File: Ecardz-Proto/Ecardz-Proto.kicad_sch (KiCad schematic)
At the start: 0 parts

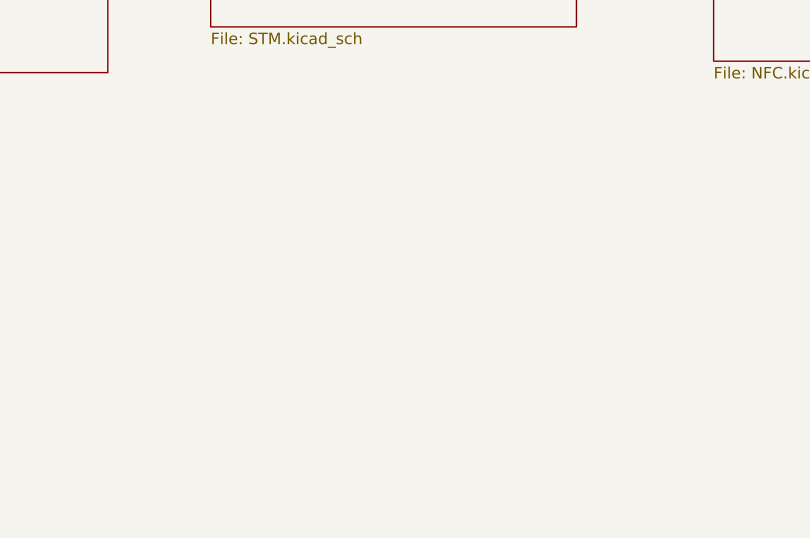
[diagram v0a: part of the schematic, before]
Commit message: added EEPROM schematic, removed personal files
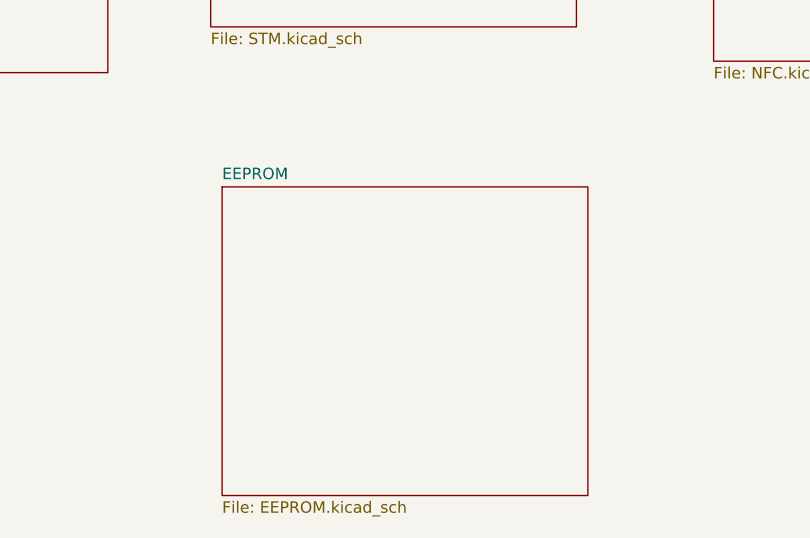
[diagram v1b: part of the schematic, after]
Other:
- added sheet EEPROM (EEPROM.kicad_sch)
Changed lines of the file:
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@@
+	)
+	(sheet
+		(at 114.3 115.57)
+		(size 40.64 34.29)
+		(fields_autoplaced yes)
+		(stroke
+			(width 0.1524)
+			(type solid)
+		)
+		(fill
+			(color 0 0 0 0.0000)
+		)
+		(property "Sheetname" "EEPROM"
+			(at 114.3 114.8584 0)
+			(effects
+				(font
+					(size 1.27 1.27)
+				)
+				(justify left bottom)
+			)
+		)
+		(property "Sheetfile" "EEPROM.kicad_sch"
+			(at 114.3 150.4446 0)
+			(effects
+				(font
+					(size 1.27 1.27)
+				)
+				(justify left top)
+			)
+		)
+		(instances
+			(project "Ecardz-Proto"
+				(path "/2adbba85-9270-4efb-857d-656bb51406ca"
+					(page "5")
+				)
+			)
+		)
 	)
 	(sheet

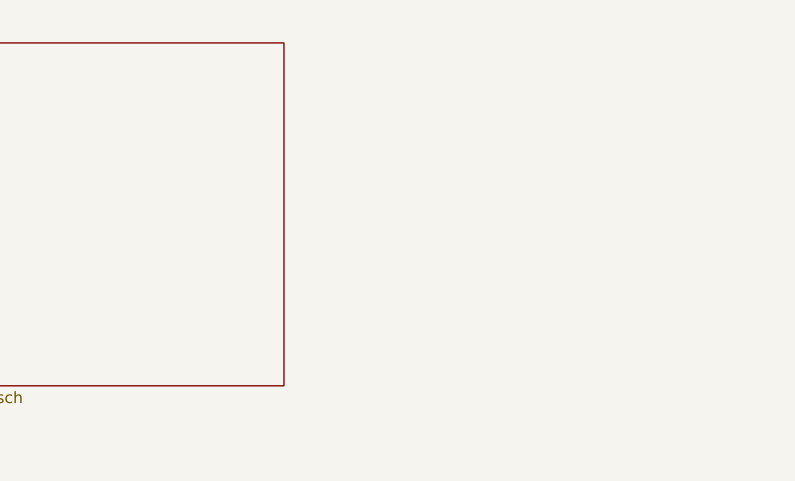
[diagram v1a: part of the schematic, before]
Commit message: added energy harvesting schematic page
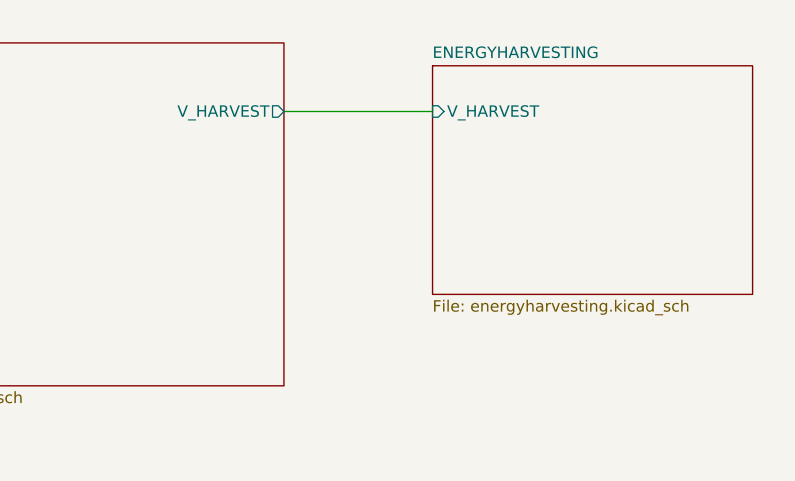
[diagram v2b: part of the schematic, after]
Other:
- added sheet ENERGYHARVESTING (energyharvesting.kicad_sch)
- sheet NFC ports: added V_HARVEST; removed none
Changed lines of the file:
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@@
+	(wire
+		(pts
+			(xy 214.63 71.12) (xy 231.14 71.12)
+		)
+		(stroke
+			(width 0)
+			(type default)
+		)
+	)
 	(wire
 		(pts
@@
 	)
 	(sheet
+		(at 231.14 66.04)
+		(size 35.56 25.4)
+		(fields_autoplaced yes)
+		(stroke
+			(width 0.1524)
+			(type solid)
+		)
+		(fill
+			(color 0 0 0 0.0000)
+		)
+		(property "Sheetname" "ENERGYHARVESTING"
+			(at 231.14 65.3284 0)
+			(effects
+				(font
+					(size 1.27 1.27)
+				)
+				(justify left bottom)
+			)
+		)
+		(property "Sheetfile" "energyharvesting.kicad_sch"
+			(at 231.14 92.0246 0)
+			(effects
+				(font
+					(size 1.27 1.27)
+				)
+				(justify left top)
+			)
+		)
+		(pin "V_HARVEST" input
+			(at 231.14 71.12 180)
+			(effects
+				(font
+					(size 1.27 1.27)
+				)
+				(justify left)
+			)
+		)
+		(instances
+			(project "Ecardz-Proto"
+				(path "/2adbba85-9270-4efb-857d-656bb51406ca"
+					(page "6")
+				)
+			)
+		)
+	)
+	(sheet
 		(at 168.91 63.5)
 		(size 45.72 38.1)
@@
 			)
 		)
+		(pin "V_HARVEST" output
+			(at 214.63 71.12 0)
+			(effects
+				(font
+					(size 1.27 1.27)
+				)
+				(justify right)
+			)
+		)

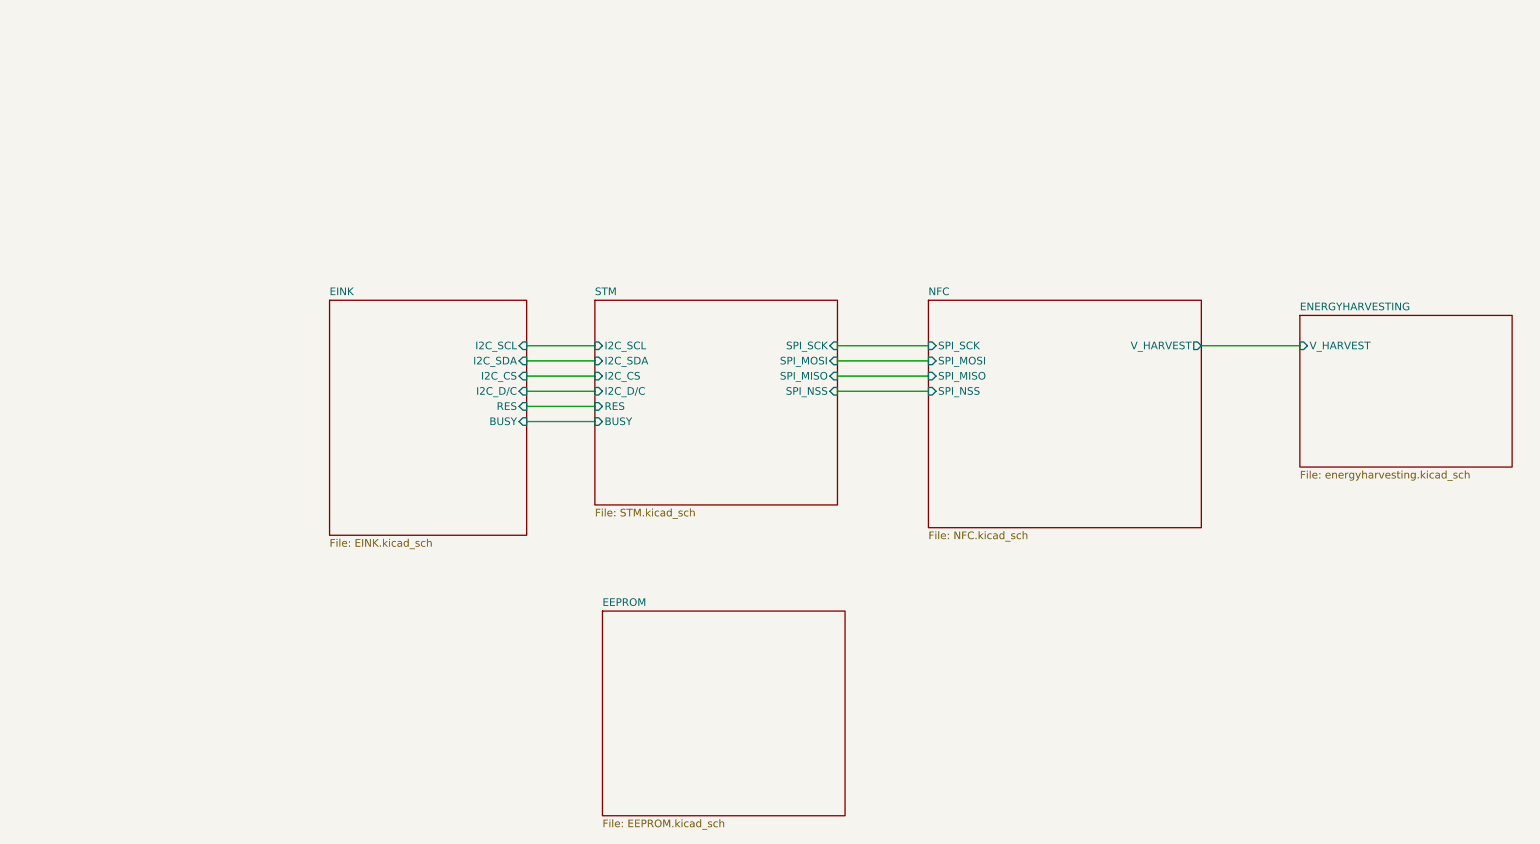
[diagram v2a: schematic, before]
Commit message: added energy harvesting sensing ADC to NFC
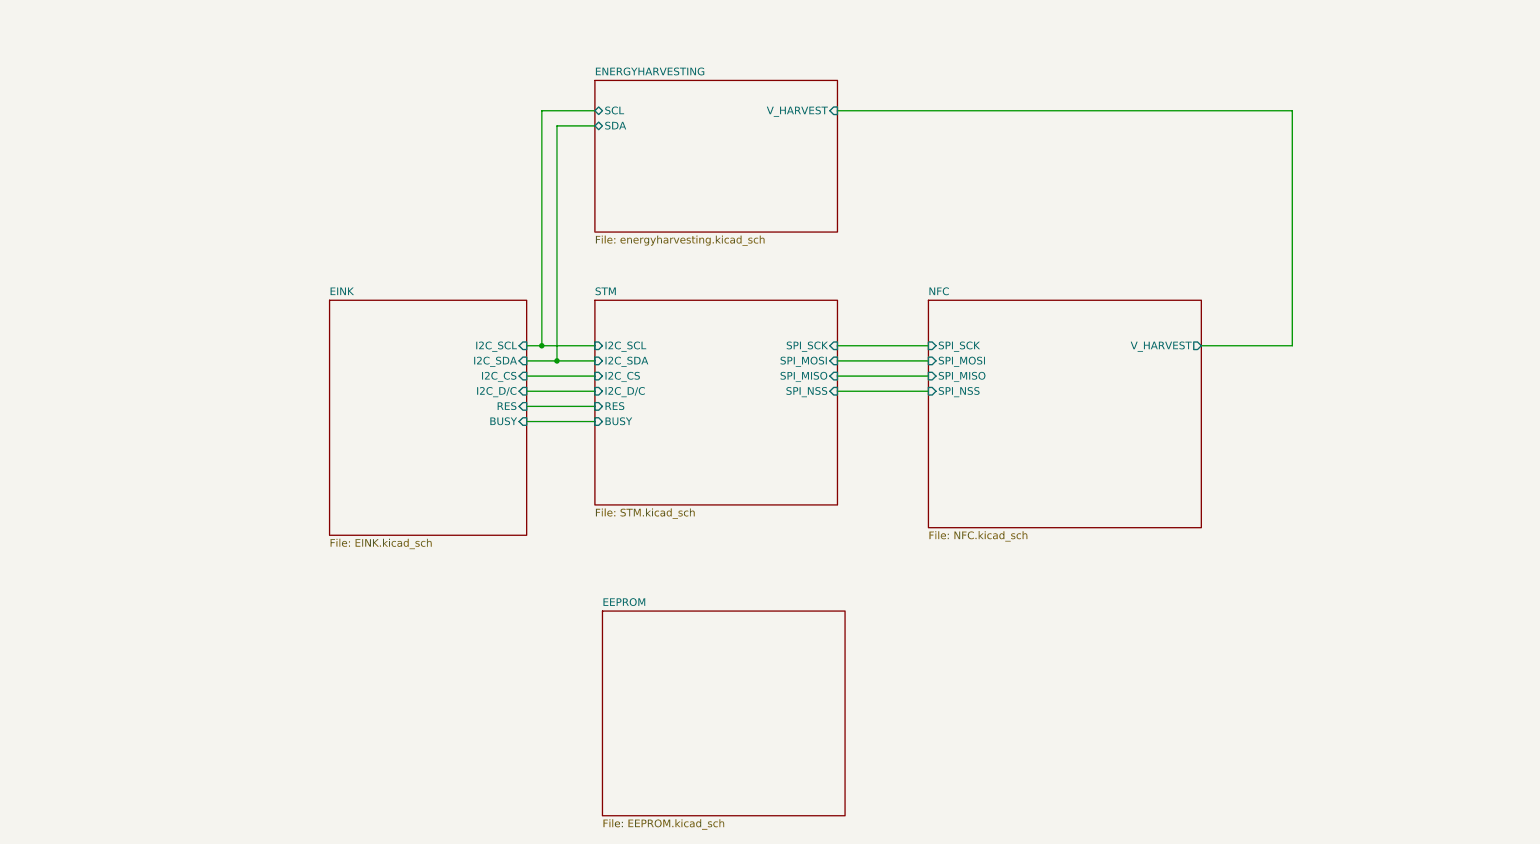
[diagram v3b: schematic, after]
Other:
- sheet ENERGYHARVESTING ports: added SCL, SDA; removed none
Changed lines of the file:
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@@
 	(generator_version "8.0")
 	(paper "A4")
-	(wire
-		(pts
-			(xy 101.6 73.66) (xy 113.03 73.66)
+	(junction
+		(at 106.68 73.66)
+		(diameter 0)
+		(color 0 0 0 0)
+	)
+	(junction
+		(at 104.14 71.12)
+		(diameter 0)
+		(color 0 0 0 0)
+	)
+	(wire
+		(pts
+			(xy 101.6 73.66) (xy 106.68 73.66)
 		)
 		(stroke
@@
 	(wire
 		(pts
-			(xy 101.6 71.12) (xy 113.03 71.12)
+			(xy 113.03 34.29) (xy 106.68 34.29)
+		)
+		(stroke
+			(width 0)
+			(type default)
+		)
+	)
+	(wire
+		(pts
+			(xy 153.67 31.75) (xy 229.87 31.75)
+		)
+		(stroke
+			(width 0)
+			(type default)
+		)
+	)
+	(wire
+		(pts
+			(xy 106.68 34.29) (xy 106.68 73.66)
+		)
+		(stroke
+			(width 0)
+			(type default)
+		)
+	)
+	(wire
+		(pts
+			(xy 229.87 31.75) (xy 229.87 71.12)
+		)
+		(stroke
+			(width 0)
+			(type default)
+		)
+	)
+	(wire
+		(pts
+			(xy 229.87 71.12) (xy 214.63 71.12)
+		)
+		(stroke
+			(width 0)
+			(type default)
+		)
+	)
+	(wire
+		(pts
+			(xy 101.6 71.12) (xy 104.14 71.12)
+		)
+		(stroke
+			(width 0)
+			(type default)
+		)
+	)
+	(wire
+		(pts
+			(xy 104.14 71.12) (xy 113.03 71.12)
 		)
 		(stroke
@@
 	(wire
 		(pts
-			(xy 214.63 71.12) (xy 231.14 71.12)
+			(xy 104.14 31.75) (xy 113.03 31.75)
 		)
 		(stroke
@@
 	(wire
 		(pts
+			(xy 106.68 73.66) (xy 113.03 73.66)
+		)
+		(stroke
+			(width 0)
+			(type default)
+		)
+	)
+	(wire
+		(pts
 			(xy 153.67 78.74) (xy 168.91 78.74)
 		)
@@
 		(pts
 			(xy 101.6 78.74) (xy 113.03 78.74)
+		)
+		(stroke
+			(width 0)
+			(type default)
+		)
+	)
+	(wire
+		(pts
+			(xy 104.14 31.75) (xy 104.14 71.12)
 		)
 		(stroke
@@
 	)
 	(sheet
-		(at 231.14 66.04)
-		(size 35.56 25.4)
+		(at 113.03 26.67)
+		(size 40.64 25.4)
 		(fields_autoplaced yes)
 		(stroke
@@
 		)
 		(property "Sheetname" "ENERGYHARVESTING"
-			(at 231.14 65.3284 0)
+			(at 113.03 25.9584 0)
 			(effects
 				(font
@@
 		)
 		(property "Sheetfile" "energyharvesting.kicad_sch"
-			(at 231.14 92.0246 0)
+			(at 113.03 52.6546 0)
 			(effects
 				(font
@@
 		)
 		(pin "V_HARVEST" input
-			(at 231.14 71.12 180)
-			(effects
-				(font
+			(at 153.67 31.75 0)
+			(effects
+				(font
+					(size 1.27 1.27)
+				)
+				(justify right)
+			)
+		)
+		(pin "SCL" bidirectional
+			(at 113.03 31.75 180)
+			(effects
+				(font
+					(size 1.27 1.27)
+				)
+				(justify left)
+			)
+		)
+		(pin "SDA" bidirectional
+			(at 113.03 34.29 180)
+			(effects
+				(font

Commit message: removed eeprom
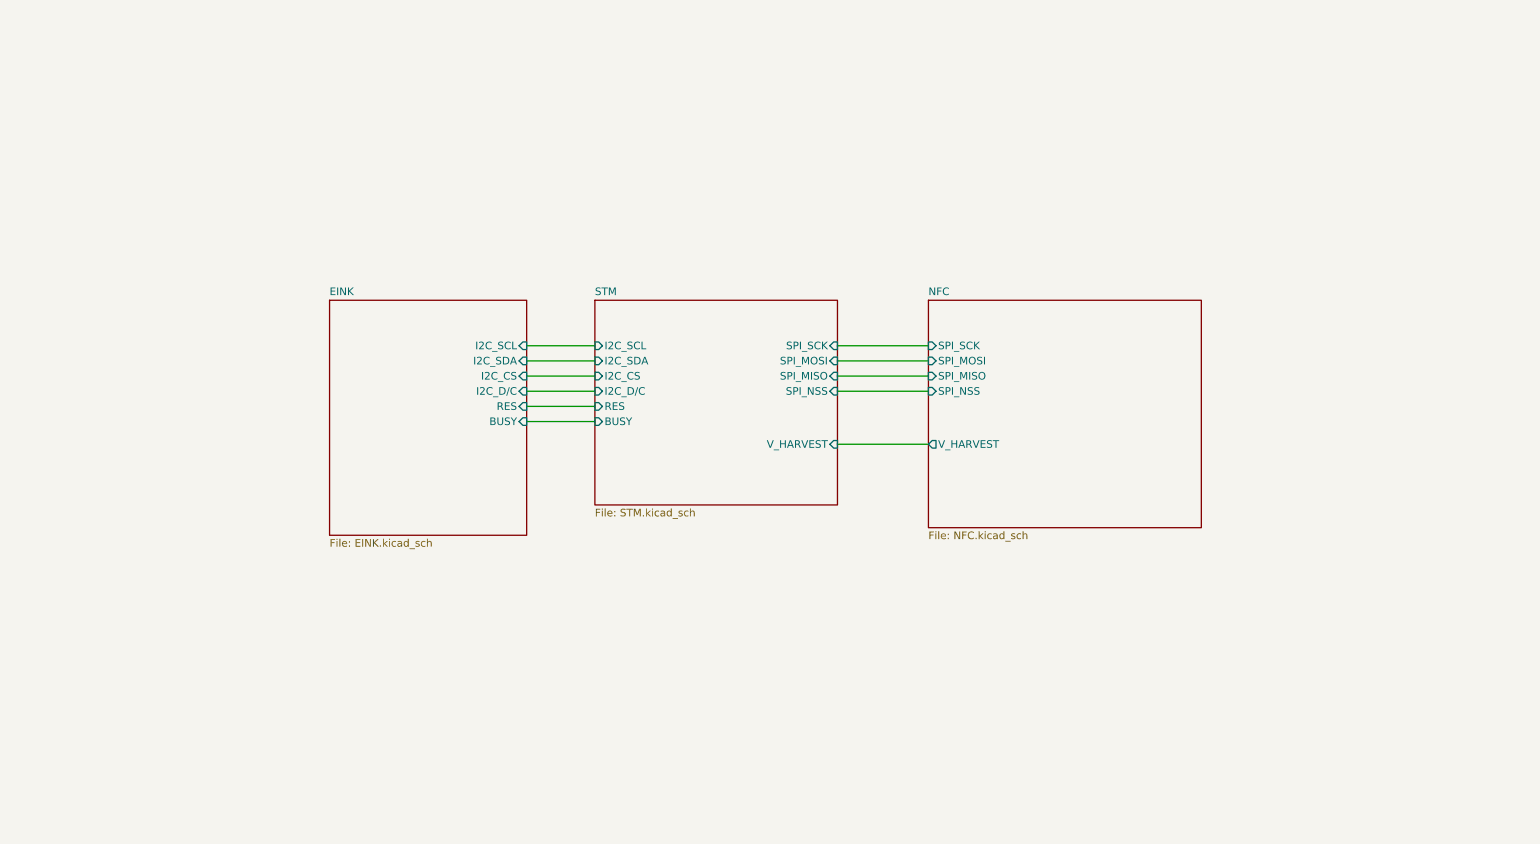
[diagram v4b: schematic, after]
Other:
- removed sheet EEPROM
- removed sheet ENERGYHARVESTING
- sheet STM ports: added V_HARVEST; removed none
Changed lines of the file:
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@@
 	(generator_version "8.0")
 	(paper "A4")
-	(junction
-		(at 106.68 73.66)
-		(diameter 0)
-		(color 0 0 0 0)
-	)
-	(junction
-		(at 104.14 71.12)
-		(diameter 0)
-		(color 0 0 0 0)
-	)
-	(wire
-		(pts
-			(xy 101.6 73.66) (xy 106.68 73.66)
-		)
-		(stroke
-			(width 0)
-			(type default)
-		)
-	)
 	(wire
 		(pts
@@
 	(wire
 		(pts
-			(xy 113.03 34.29) (xy 106.68 34.29)
-		)
-		(stroke
-			(width 0)
-			(type default)
-		)
-	)
-	(wire
-		(pts
-			(xy 153.67 31.75) (xy 229.87 31.75)
-		)
-		(stroke
-			(width 0)
-			(type default)
-		)
-	)
-	(wire
-		(pts
-			(xy 106.68 34.29) (xy 106.68 73.66)
-		)
-		(stroke
-			(width 0)
-			(type default)
-		)
-	)
-	(wire
-		(pts
-			(xy 229.87 31.75) (xy 229.87 71.12)
-		)
-		(stroke
-			(width 0)
-			(type default)
-		)
-	)
-	(wire
-		(pts
-			(xy 229.87 71.12) (xy 214.63 71.12)
-		)
-		(stroke
-			(width 0)
-			(type default)
-		)
-	)
-	(wire
-		(pts
-			(xy 101.6 71.12) (xy 104.14 71.12)
-		)
-		(stroke
-			(width 0)
-			(type default)
-		)
-	)
-	(wire
-		(pts
-			(xy 104.14 71.12) (xy 113.03 71.12)
+			(xy 153.67 87.63) (xy 168.91 87.63)
+		)
+		(stroke
+			(width 0)
+			(type default)
+		)
+	)
+	(wire
+		(pts
+			(xy 101.6 71.12) (xy 113.03 71.12)
 		)
 		(stroke
@@
 	(wire
 		(pts
-			(xy 104.14 31.75) (xy 113.03 31.75)
-		)
-		(stroke
-			(width 0)
-			(type default)
-		)
-	)
-	(wire
-		(pts
 			(xy 101.6 83.82) (xy 113.03 83.82)
 		)
@@
 	(wire
 		(pts
-			(xy 106.68 73.66) (xy 113.03 73.66)
+			(xy 101.6 73.66) (xy 113.03 73.66)
 		)
 		(stroke
@@
 	(wire
 		(pts
-			(xy 104.14 31.75) (xy 104.14 71.12)
-		)
-		(stroke
-			(width 0)
-			(type default)
-		)
-	)
-	(wire
-		(pts
 			(xy 153.67 71.12) (xy 168.91 71.12)
 		)
@@
 			(width 0)
 			(type default)
-		)
-	)
-	(sheet
-		(at 114.3 115.57)
-		(size 40.64 34.29)
-		(fields_autoplaced yes)
-		(stroke
-			(width 0.1524)
-			(type solid)
-		)
-		(fill
-			(color 0 0 0 0.0000)
-		)
-		(property "Sheetname" "EEPROM"
-			(at 114.3 114.8584 0)
-			(effects
-				(font
-					(size 1.27 1.27)
-				)
-				(justify left bottom)
-			)
-		)
-		(property "Sheetfile" "EEPROM.kicad_sch"
-			(at 114.3 150.4446 0)
-			(effects
-				(font
-					(size 1.27 1.27)
-				)
-				(justify left top)
-			)
-		)
-		(instances
-			(project "Ecardz-Proto"
-				(path "/2adbba85-9270-4efb-857d-656bb51406ca"
-					(page "5")
-				)
-			)
-		)
-	)
-	(sheet
-		(at 113.03 26.67)
-		(size 40.64 25.4)
-		(fields_autoplaced yes)
-		(stroke
-			(width 0.1524)
-			(type solid)
-		)
-		(fill
-			(color 0 0 0 0.0000)
-		)
-		(property "Sheetname" "ENERGYHARVESTING"
-			(at 113.03 25.9584 0)
-			(effects
-				(font
-					(size 1.27 1.27)
-				)
-				(justify left bottom)
-			)
-		)
-		(property "Sheetfile" "energyharvesting.kicad_sch"
-			(at 113.03 52.6546 0)
-			(effects
-				(font
-					(size 1.27 1.27)
-				)
-				(justify left top)
-			)
-		)
-		(pin "V_HARVEST" input
-			(at 153.67 31.75 0)
-			(effects
-				(font
-					(size 1.27 1.27)
-				)
-				(justify right)
-			)
-		)
-		(pin "SCL" bidirectional
-			(at 113.03 31.75 180)
-			(effects
-				(font
-					(size 1.27 1.27)
-				)
-				(justify left)
-			)
-		)
-		(pin "SDA" bidirectional
-			(at 113.03 34.29 180)
-			(effects
-				(font
-					(size 1.27 1.27)
-				)
-				(justify left)
-			)
-		)
-		(instances
-			(project "Ecardz-Proto"
-				(path "/2adbba85-9270-4efb-857d-656bb51406ca"
-					(page "6")
-				)
-			)
 		)
 	)
@@
 		)
 		(pin "V_HARVEST" output
-			(at 214.63 71.12 0)
-			(effects
-				(font
-					(size 1.27 1.27)
-				)
-				(justify right)
+			(at 168.91 87.63 180)
+			(effects
+				(font
+					(size 1.27 1.27)
+				)
+				(justify left)
 			)
 		)
@@
 			(effects
 				(font
+					(size 1.27 1.27)
+				)
+				(justify right)
+			)
+		)
+		(pin "V_HARVEST" input
+			(at 153.67 87.63 0)
+			(effects
+				(font
